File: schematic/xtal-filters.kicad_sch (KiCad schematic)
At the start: 38 parts, among them Y10 9.000, Y11 9.000, Y12 9.000, Y13 9.000, Y14 9.000, Y15 9.000, Y16 9.000, Y17 9.000, Y18 9.000, Y4 9.000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

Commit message: Schematic: minor fixes
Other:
- note added: "10T bifilar @ FT37-43"
- note removed: "10T bifilar @ T37-43"
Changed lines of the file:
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@@
     (effects (font (size 1.27 1.27)) (justify left bottom))
   )
-  (text "10T bifilar\n@ T37-43" (at 201.295 107.315 0)
+  (text "10T bifilar\n@ FT37-43" (at 201.295 107.315 0)
     (effects (font (size 1.27 1.27)) (justify left bottom))
   )
-  (text "10T bifilar\n@ T37-43" (at 86.995 106.68 0)
+  (text "10T bifilar\n@ FT37-43" (at 86.995 106.68 0)
     (effects (font (size 1.27 1.27)) (justify left bottom))
   )

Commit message: Schematic: add a bit more 0.1u capacitors
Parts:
- added C168: 0.1u, symbol Device:C
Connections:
- net GND: now also C168.2
- net SSB_GND: now also C168.1
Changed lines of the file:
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@@
   (junction (at 167.64 79.375) (diameter 0) (color 0 0 0 0)
+  )
+  (junction (at 57.785 128.905) (diameter 0) (color 0 0 0 0)
   )
   (junction (at 240.665 99.695) (diameter 0) (color 0 0 0 0)
@@
     (stroke (width 0) (type default))
   )
+  (wire (pts (xy 57.785 128.905) (xy 57.785 135.89))
+    (stroke (width 0) (type default))
+  )
   (wire (pts (xy 132.08 79.375) (xy 132.08 84.455))
     (stroke (width 0) (type default))
@@
   )
   (wire (pts (xy 31.115 112.395) (xy 34.29 112.395))
+    (stroke (width 0) (type default))
+  )
+  (wire (pts (xy 57.785 143.51) (xy 57.785 146.685))
     (stroke (width 0) (type default))
   )
@@
     )
   )
+  (symbol (lib_id "Device:C") (at 57.785 139.7 0) (unit 1)
+    (in_bom yes) (on_board yes) (dnp no) (fields_autoplaced)
+    (property "Reference" "C168" (at 61.595 138.43 0)
+      (effects (font (size 1.27 1.27)) (justify left))
+    )
+    (property "Value" "0.1u" (at 61.595 140.97 0)
+      (effects (font (size 1.27 1.27)) (justify left))
+    )
+    (property "Footprint" "" (at 58.7502 143.51 0)
+      (effects (font (size 1.27 1.27)) hide)
+    )
+    (property "Datasheet" "~" (at 57.785 139.7 0)
+      (effects (font (size 1.27 1.27)) hide)
+    )
+    (pin "1")
+    (pin "2")
+    (instances
+      (project "hbr-mk2"
+        (path "/700c9878-4ed7-49d5-a273-77cf9d92989d/4a33e42c-b3be-4c3a-afde-bb63d1cdac9b"
+          (reference "C168") (unit 1)
+        )
+      )
+    )
+  )
   (symbol (lib_id "Diode:1N4148") (at 41.91 84.455 0) (unit 1)
     (in_bom yes) (on_board yes) (dnp no) (fields_autoplaced)
@@
         )
       )
+    )
+  )
+  (symbol (lib_id "power:GND") (at 57.785 146.685 0) (unit 1)
+    (in_bom yes) (on_board yes) (dnp no) (fields_autoplaced)
+    (property "Reference" "#PWR0150" (at 57.785 153.035 0)
+      (effects (font (size 1.27 1.27)) hide)
+    )
+    (property "Value" "GND" (at 57.785 151.765 0)
+      (effects (font (size 1.27 1.27)) hide)
+    )
+    (property "Footprint" "" (at 57.785 146.685 0)
+      (effects (font (size 1.27 1.27)) hide)
+    )
+    (property "Datasheet" "" (at 57.785 146.685 0)
+      (effects (font (size 1.27 1.27)) hide)
+    )
+    (pin "1")
+    (instances
+      (project "hbr-mk2"
+        (path "/700c9878-4ed7-49d5-a273-77cf9d92989d/4a33e42c-b3be-4c3a-afde-bb63d1cdac9b"
+          (reference "#PWR0150") (unit 1)
+        )
+      )

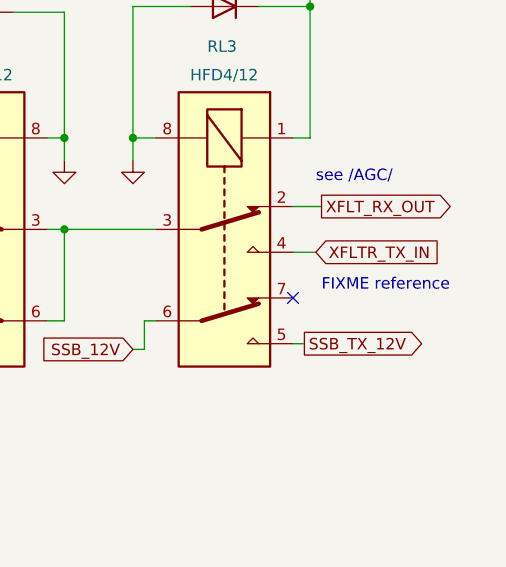
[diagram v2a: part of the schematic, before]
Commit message: Add /TX SSB/ sheet
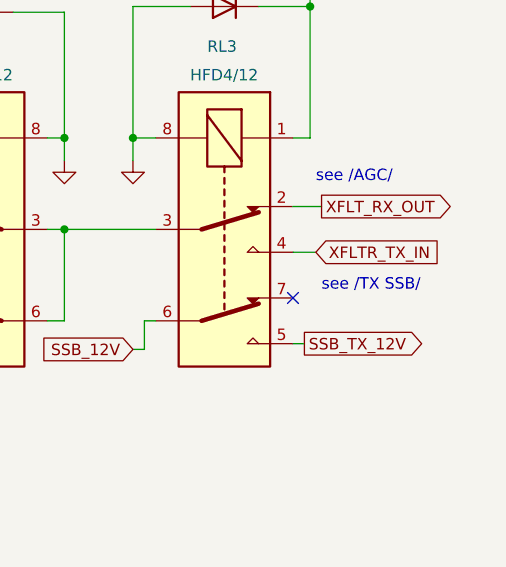
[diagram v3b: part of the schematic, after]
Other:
- note added: "see /TX SSB/"
- note removed: "FIXME reference"
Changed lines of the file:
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@@
     (effects (font (size 1.27 1.27)) (justify left bottom))
   )
-  (text "FIXME reference" (at 269.24 116.84 0)
+  (text "see /TX SSB/" (at 269.24 116.84 0)
     (effects (font (size 1.27 1.27)) (justify left bottom))
   )

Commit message: Minor changes
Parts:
- renumbered L12 to L13, RL3 to RL4, RL3 to RL5, RL3 to RL6
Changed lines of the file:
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@@
     (instances
       (project "hbr-mk2"
-        (path "/700c9878-4ed7-49d5-a273-77cf9d92989d/f830f485-dae1-49b8-8b15-2f9b2d30db58"
-          (reference "RL3") (unit 1)
-        )
         (path "/700c9878-4ed7-49d5-a273-77cf9d92989d/4a33e42c-b3be-4c3a-afde-bb63d1cdac9b"
           (reference "RL3") (unit 1)
@@
   (symbol (lib_id "Relay:G2RL-2-ASI-DC5") (at 231.14 109.855 90) (mirror x) (unit 1)
     (in_bom yes) (on_board yes) (dnp no)
-    (property "Reference" "RL3" (at 233.045 89.535 90)
+    (property "Reference" "RL4" (at 233.045 89.535 90)
       (effects (font (size 1.27 1.27)) (justify left))
     )
@@
     (instances
       (project "hbr-mk2"
-        (path "/700c9878-4ed7-49d5-a273-77cf9d92989d/f830f485-dae1-49b8-8b15-2f9b2d30db58"
-          (reference "RL3") (unit 1)
-        )
         (path "/700c9878-4ed7-49d5-a273-77cf9d92989d/4a33e42c-b3be-4c3a-afde-bb63d1cdac9b"
           (reference "RL4") (unit 1)
@@
   (symbol (lib_id "Device:L_Ferrite_Coupled_1423") (at 206.375 117.475 90) (mirror x) (unit 1)
     (in_bom yes) (on_board yes) (dnp no)
-    (property "Reference" "L12" (at 207.645 110.49 90)
+    (property "Reference" "L13" (at 207.645 110.49 90)
       (effects (font (size 1.27 1.27)) (justify left))
     )
@@
     (instances
       (project "hbr-mk2"
-        (path "/700c9878-4ed7-49d5-a273-77cf9d92989d/0b45878c-17b8-4be8-9884-0f2bddd34788"
-          (reference "L12") (unit 1)
-        )
         (path "/700c9878-4ed7-49d5-a273-77cf9d92989d/4a33e42c-b3be-4c3a-afde-bb63d1cdac9b"
           (reference "L13") (unit 1)
@@
     (instances
       (project "hbr-mk2"
-        (path "/700c9878-4ed7-49d5-a273-77cf9d92989d/0b45878c-17b8-4be8-9884-0f2bddd34788"
-          (reference "L12") (unit 1)
-        )
         (path "/700c9878-4ed7-49d5-a273-77cf9d92989d/4a33e42c-b3be-4c3a-afde-bb63d1cdac9b"
           (reference "L12") (unit 1)
@@
   (symbol (lib_id "Relay:G2RL-2-ASI-DC5") (at 258.445 109.855 270) (unit 1)
     (in_bom yes) (on_board yes) (dnp no)
-    (property "Reference" "RL3" (at 256.54 89.535 90)
+    (property "Reference" "RL6" (at 256.54 89.535 90)
       (effects (font (size 1.27 1.27)) (justify left))
     )
@@
     (instances
       (project "hbr-mk2"
-        (path "/700c9878-4ed7-49d5-a273-77cf9d92989d/f830f485-dae1-49b8-8b15-2f9b2d30db58"
-          (reference "RL3") (unit 1)
-        )
         (path "/700c9878-4ed7-49d5-a273-77cf9d92989d/4a33e42c-b3be-4c3a-afde-bb63d1cdac9b"
           (reference "RL6") (unit 1)
@@
   (symbol (lib_id "Relay:G2RL-2-ASI-DC5") (at 41.91 109.855 90) (mirror x) (unit 1)
     (in_bom yes) (on_board yes) (dnp no)
-    (property "Reference" "RL3" (at 43.815 89.535 90)
+    (property "Reference" "RL5" (at 43.815 89.535 90)
       (effects (font (size 1.27 1.27)) (justify left))
     )
@@
     (instances
       (project "hbr-mk2"
-        (path "/700c9878-4ed7-49d5-a273-77cf9d92989d/f830f485-dae1-49b8-8b15-2f9b2d30db58"
-          (reference "RL3") (unit 1)
-        )
         (path "/700c9878-4ed7-49d5-a273-77cf9d92989d/4a33e42c-b3be-4c3a-afde-bb63d1cdac9b"
           (reference "RL5") (unit 1)
